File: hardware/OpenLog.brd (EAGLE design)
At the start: 17.8 x 19.1 mm, 20 parts, among them Q1 16MHZ, U1 ATMEGA328P_TQFP, U2 3.3V MIC5205, U3 microSD Socket

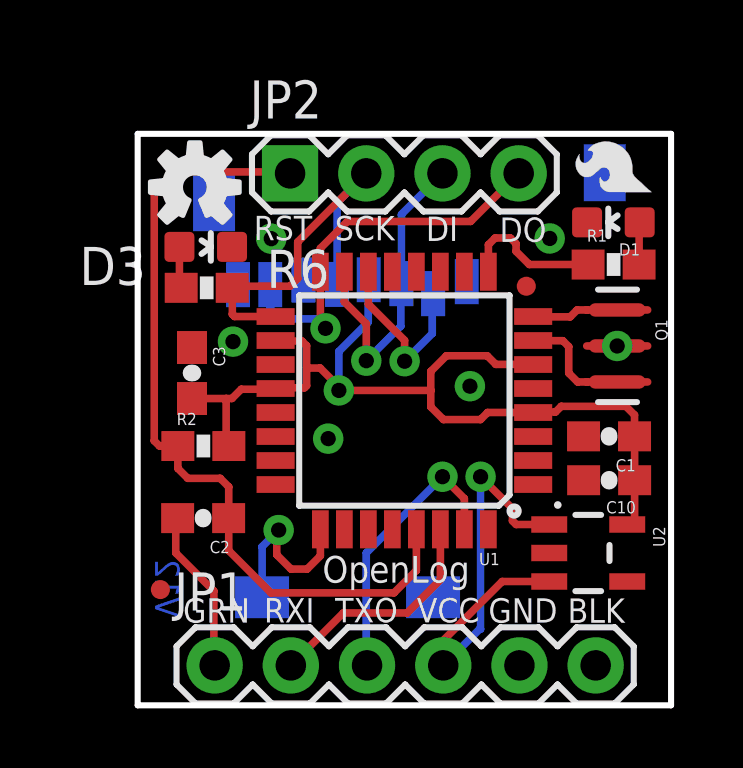
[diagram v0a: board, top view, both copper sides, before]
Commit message: Added Test point , removed OSHW logo
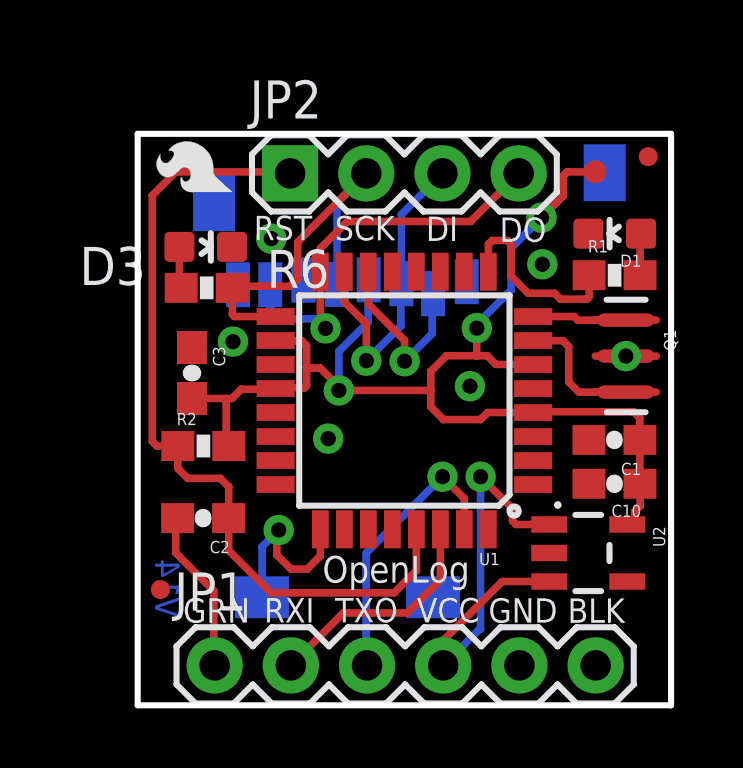
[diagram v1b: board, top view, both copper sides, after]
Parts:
- removed LOGO2: OSHW-LOGOS, SparkFun-Aesthetics:OSHW-LOGO-S
- added TP1: TEST-POINT3, SparkFun-Passives:PAD.03X.03
- moved LOGO1 14.0 mm to (22.6, 6.63)
- moved FID1 5.93 mm to (36.1, 8.13)
- moved Q1 0.44 mm to (35.3, 1.48)
- moved D1 0.38 mm to (35.0, 5.56)
- moved R1 0.36 mm to (34.9, 4.18)
- moved C1 0.21 mm to (34.9, -1.31)
- moved C10 0.21 mm to (34.9, -2.78)
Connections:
- net 3.3V: now also TP1.P$1
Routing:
- net 3.3V: track 32.8 -> 41.3 mm, vias 1 -> 3
- net N$4: track 4.83 -> 6.51 mm
- net N$1: track 1.89 -> 3.14 mm
- net N$2: track 2.87 -> 3.48 mm
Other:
- board text added: "V14"
- board text removed: "V12"

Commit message: Headers moved on grid.
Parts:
- moved JP1 0.07 mm to (21.6, -8.89)
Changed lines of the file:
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@@
 <setting verticaltext="up"/>
 </settings>
-<grid distance="0.05" unitdist="inch" unit="inch" style="lines" multiple="1" display="yes" altdistance="0.0001" altunitdist="inch" altunit="inch"/>
+<grid distance="0.05" unitdist="inch" unit="inch" style="lines" multiple="1" display="yes" altdistance="0.005" altunitdist="inch" altunit="inch"/>
 <layers>
 <layer number="1" name="Top" color="4" fill="1" visible="yes" active="yes"/>
@@
 <layer number="47" name="Measures" color="7" fill="1" visible="no" active="yes"/>
 <layer number="48" name="Document" color="7" fill="1" visible="no" active="yes"/>
-<layer number="49" name="Reference" color="7" fill="1" visible="yes" active="yes"/>
+<layer number="49" name="Reference" color="7" fill="1" visible="no" active="yes"/>
 <layer number="50" name="dxf" color="7" fill="1" visible="no" active="yes"/>
 <layer number="51" name="tDocu" color="6" fill="1" visible="yes" active="yes"/>
@@
 <attribute name="PROD_ID" value="XTAL-08900" x="35.321240625" y="1.48081875" size="1.778" layer="27" rot="R270" display="off"/>
 </element>
-<element name="JP1" library="SparkFun" package="1X06" value="Serial Connection" x="21.6154" y="-8.8290375"/>
+<element name="JP1" library="SparkFun" package="1X06" value="Serial Connection" x="21.59" y="-8.89"/>
 <element name="C2" library="SparkFun-Capacitors" package="0603-CAP" value="0.1uF" x="21.231859375" y="-3.919221875" rot="R180">
 <attribute name="PROD_ID" value="CAP-00810" x="21.231859375" y="-3.919221875" size="1.778" layer="27" rot="R180" display="off"/>
@@
 <attribute name="VALUE" value="1.0uF" x="34.9402375" y="-1.313175" size="1.778" layer="27" rot="R180" display="off"/>
 </element>
-<element name="JP2" library="SparkFun" package="1X04" value="" x="24.13" y="7.571740625"/>
+<element name="JP2" library="SparkFun" package="1X04" value="" x="24.13" y="7.62"/>
 <element name="U1" library="SparkFun-DigitalIC" package="TQFP32-08" value="ATMEGA328P_TQFP" x="27.94" y="0" rot="R180">
 <attribute name="PROD_ID" value="IC-09069" x="27.94" y="0" size="0.8128" layer="27" font="vector" ratio="15" rot="R180" display="off"/>
@@
 <contactref element="U1" pad="17"/>
 <wire x1="22.204678125" y1="3.753225" x2="22.201240625" y2="3.7566625" width="0.254" layer="1"/>
-<wire x1="25.69464375" y1="3.870953125" x2="25.69464375" y2="6.596384375" width="0.254" layer="16"/>
-<wire x1="25.69464375" y1="6.596384375" x2="26.67" y2="7.571740625" width="0.254" layer="16"/>
-<wire x1="24.384" y1="4.064" x2="24.384" y2="5.285740625" width="0.254" layer="1"/>
-<wire x1="24.384" y1="5.285740625" x2="26.67" y2="7.571740625" width="0.254" layer="1"/>
+<wire x1="25.69464375" y1="3.870953125" x2="25.69464375" y2="6.64464375" width="0.254" layer="16"/>
+<wire x1="24.384" y1="4.064" x2="24.384" y2="5.334" width="0.254" layer="1"/>
 <wire x1="23.6474" y1="2.8" x2="22.2799625" y2="2.8" width="0.254" layer="1"/>
 <wire x1="22.2799625" y1="2.8" x2="22.20468125" y2="2.87528125" width="0.254" layer="1"/>
@@
 <wire x1="24.13" y1="3.81" x2="22.254578125" y2="3.81" width="0.254" layer="1"/>
 <wire x1="22.254578125" y1="3.81" x2="22.201240625" y2="3.7566625" width="0.254" layer="1"/>
+<wire x1="24.384" y1="5.334" x2="26.67" y2="7.62" width="0.254" layer="1"/>
+<wire x1="25.69464375" y1="6.64464375" x2="26.67" y2="7.62" width="0.254" layer="16"/>
 </signal>
 <signal name="MISO">
@@
 <contactref element="U1" pad="16"/>
 <wire x1="25.14" y1="5.074" x2="25.14" y2="4.2926" width="0.254" layer="1"/>
-<wire x1="30.147259375" y1="5.969" x2="31.75" y2="7.571740625" width="0.254" layer="1"/>
 <wire x1="23.45181875" y1="3.086103125" x2="23.815040625" y2="2.72288125" width="0.254" layer="16"/>
 <wire x1="23.815040625" y1="2.72288125" x2="24.99360625" y2="2.72288125" width="0.254" layer="16"/>
@@
 <wire x1="23.45181875" y1="3.086103125" x2="23.45181875" y2="3.846415625" width="0.254" layer="16"/>
 <wire x1="23.45181875" y1="3.846415625" x2="23.4672125" y2="3.861809375" width="0.254" layer="16"/>
+<wire x1="30.147259375" y1="5.969" x2="30.147259375" y2="6.017259375" width="0.254" layer="1"/>
+<wire x1="30.147259375" y1="6.017259375" x2="31.75" y2="7.62" width="0.254" layer="1"/>
 </signal>
 <signal name="MOSI">
@@
 <wire x1="27.82149375" y1="2.479915625" x2="27.82149375" y2="3.876034375" width="0.254" layer="16"/>
 <wire x1="27.82149375" y1="3.876034375" x2="27.8418125" y2="3.896353125" width="0.254" layer="16"/>
-<wire x1="27.8418125" y1="3.896353125" x2="27.8418125" y2="6.203553125" width="0.254" layer="16"/>
-<wire x1="27.8418125" y1="6.203553125" x2="29.21" y2="7.571740625" width="0.254" layer="16"/>
+<wire x1="27.8418125" y1="3.896353125" x2="27.8418125" y2="6.2518125" width="0.254" layer="16"/>
+<wire x1="27.8418125" y1="6.2518125" x2="29.21" y2="7.62" width="0.254" layer="16"/>
 </signal>
 <signal name="N$7">
@@
 <contactref element="U1" pad="31"/>
 <wire x1="29.94" y1="-3.27" x2="29.94" y2="-4.2926" width="0.254" layer="1"/>
-<wire x1="26.67" y1="-5.08" x2="26.67" y2="-8.8036375" width="0.254" layer="16"/>
-<wire x1="26.67" y1="-8.8036375" x2="26.6954" y2="-8.8290375" width="0.254" layer="16"/>
+<wire x1="26.67" y1="-5.08" x2="26.67" y2="-8.89" width="0.254" layer="16"/>
 </signal>
 <signal name="RAW" class="1">
@@
 <wire x1="31.54171875" y1="-3.60171875" x2="30.48" y2="-2.54" width="0.254" layer="1"/>
 <wire x1="30.48" y1="-7.62" x2="30.4444375" y2="-7.62" width="0.254" layer="16"/>
-<wire x1="30.4444375" y1="-7.62" x2="29.2354" y2="-8.8290375" width="0.254" layer="16"/>
-<wire x1="29.2354" y1="-8.8290375" x2="29.2354" y2="-7.99591875" width="0.254" layer="1"/>
 <wire x1="29.2354" y1="-7.99591875" x2="31.19881875" y2="-6.0325" width="0.254" layer="1"/>
 <wire x1="31.19881875" y1="-6.0325" x2="32.76888125" y2="-6.0325" width="0.254" layer="1"/>
 <wire x1="32.76888125" y1="-6.0325" x2="32.768921875" y2="-6.032540625" width="0.254" layer="1"/>
+<wire x1="29.2354" y1="-7.99591875" x2="29.2354" y2="-8.8646" width="0.254" layer="1"/>
+<wire x1="29.2354" y1="-8.8646" x2="29.21" y2="-8.89" width="0.254" layer="1"/>
+<wire x1="30.4444375" y1="-7.62" x2="30.4444375" y2="-7.6555625" width="0.254" layer="16"/>
+<wire x1="30.4444375" y1="-7.6555625" x2="29.21" y2="-8.89" width="0.254" layer="16"/>
 </signal>
 <signal name="N$1">
@@
 <wire x1="20.32" y1="-5.08" x2="20.32" y2="-3.98108125" width="0.254" layer="1"/>
 <wire x1="20.32" y1="-3.98108125" x2="20.381859375" y2="-3.919221875" width="0.254" layer="1"/>
-<wire x1="21.59" y1="-6.35" x2="21.59" y2="-8.8036375" width="0.254" layer="1"/>
-<wire x1="21.59" y1="-8.8036375" x2="21.6154" y2="-8.8290375" width="0.254" layer="1"/>
+<wire x1="21.59" y1="-6.35" x2="21.59" y2="-8.89" width="0.254" layer="1"/>
 </signal>
 <signal name="RXI">
@@
 <wire x1="29.14" y1="-5.9780375" x2="28.03651875" y2="-7.08151875" width="0.254" layer="1"/>
 <wire x1="28.03651875" y1="-7.08151875" x2="25.90291875" y2="-7.08151875" width="0.254" layer="1"/>
-<wire x1="25.90291875" y1="-7.08151875" x2="24.1554" y2="-8.8290375" width="0.254" layer="1"/>
+<wire x1="25.90291875" y1="-7.08151875" x2="25.90291875" y2="-7.11708125" width="0.254" layer="1"/>
+<wire x1="25.90291875" y1="-7.11708125" x2="24.13" y2="-8.89" width="0.254" layer="1"/>
 </signal>
 <signal name="RST">
@@
 <wire x1="22.0853" y1="-5.001259375" x2="22.0853" y2="-3.9226625" width="0.254" layer="1"/>
 <wire x1="22.0853" y1="-3.9226625" x2="22.081859375" y2="-3.919221875" width="0.254" layer="1"/>
-<wire x1="20.32" y1="7.62" x2="24.081740625" y2="7.62" width="0.254" layer="1"/>
-<wire x1="24.081740625" y1="7.62" x2="24.13" y2="7.571740625" width="0.254" layer="1"/>
+<wire x1="20.32" y1="7.62" x2="24.13" y2="7.62" width="0.254" layer="1"/>
 <wire x1="20.38948125" y1="-1.51638125" x2="19.69008125" y2="-1.51638125" width="0.254" layer="1"/>
 <wire x1="19.69008125" y1="-1.51638125" x2="19.53768125" y2="-1.36398125" width="0.254" layer="1"/>

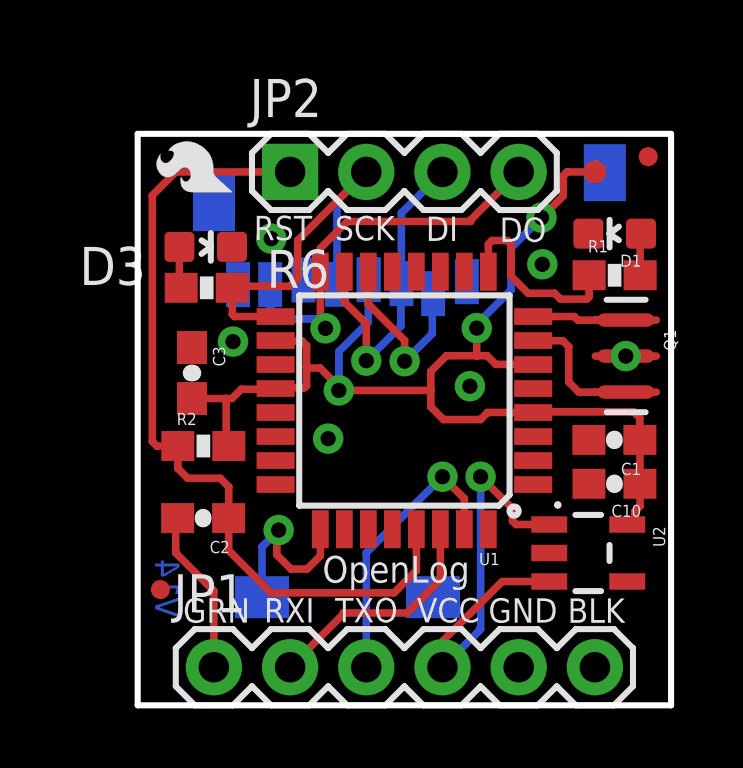
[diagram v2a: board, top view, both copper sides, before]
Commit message: Added OSHW logo, fixed trace
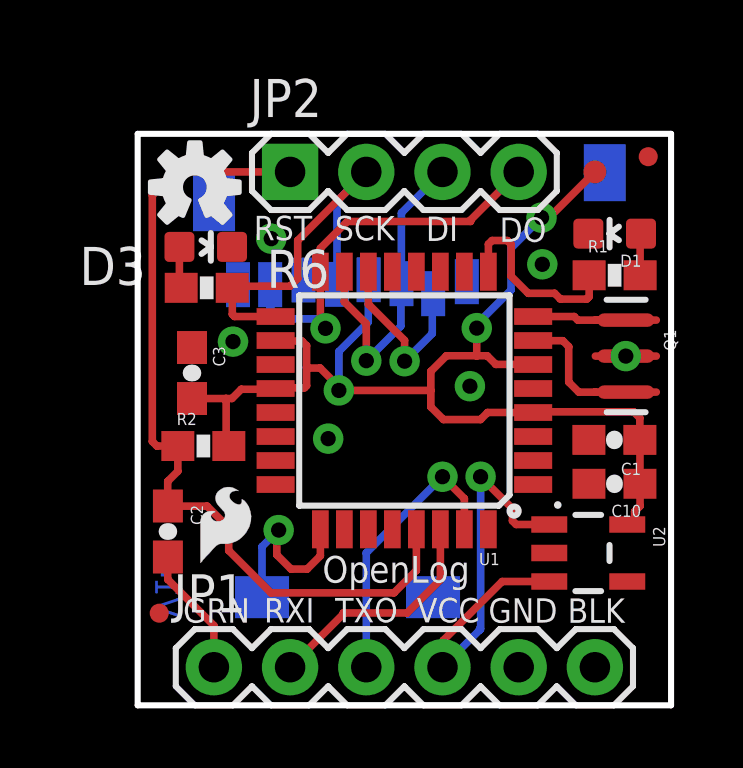
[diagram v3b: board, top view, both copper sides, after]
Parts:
- added LOGO2: OSHW-LOGOS, SparkFun-Aesthetics:OSHW-LOGO-S
- moved LOGO1 12.5 mm to (20.8, -5.78), turned to 0 degrees
- moved C2 1.26 mm to (20.1, -4.37), turned to 270 degrees
- moved FID2 0.79 mm to (19.8, -7.09)
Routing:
- net DTR: track 5.52 -> 4.31 mm
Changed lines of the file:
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@@
 <setting verticaltext="up"/>
 </settings>
-<grid distance="0.05" unitdist="inch" unit="inch" style="lines" multiple="1" display="yes" altdistance="0.005" altunitdist="inch" altunit="inch"/>
+<grid distance="0.05" unitdist="inch" unit="inch" style="lines" multiple="1" display="yes" altdistance="0.0001" altunitdist="inch" altunit="inch"/>
 <layers>
 <layer number="1" name="Top" color="4" fill="1" visible="yes" active="yes"/>
@@
 </element>
 <element name="JP1" library="SparkFun" package="1X06" value="Serial Connection" x="21.59" y="-8.89"/>
-<element name="C2" library="SparkFun-Capacitors" package="0603-CAP" value="0.1uF" x="21.231859375" y="-3.919221875" rot="R180">
-<attribute name="PROD_ID" value="CAP-00810" x="21.231859375" y="-3.919221875" size="1.778" layer="27" rot="R180" display="off"/>
-<attribute name="VALUE" value="0.1uF" x="21.231859375" y="-3.919221875" size="1.778" layer="27" rot="R180" display="off"/>
+<element name="C2" library="SparkFun-Capacitors" package="0603-CAP" value="0.1uF" x="20.058384375" y="-4.366259375" rot="R270">
+<attribute name="PROD_ID" value="CAP-00810" x="20.058384375" y="-4.366259375" size="1.778" layer="27" rot="R270" display="off"/>
+<attribute name="VALUE" value="0.1uF" x="20.058384375" y="-4.366259375" size="1.778" layer="27" rot="R270" display="off"/>
 </element>
 <element name="U3" library="SparkFun-Connectors" package="MICROSD_1:1" value="microSD Socket" x="35.1155" y="-6.9570625" rot="MR0">
@@
 <attribute name="DESIGNER" value="NAME" x="-0.742121875" y="-25.4" size="1.778" layer="27" display="off"/>
 </element>
-<element name="LOGO1" library="SparkFun-Aesthetics" package="SFE_LOGO_FLAME_.1" value="SFE_LOGO_FLAME.1_INCH" x="22.5704375" y="6.62685625" rot="R90"/>
+<element name="LOGO1" library="SparkFun-Aesthetics" package="SFE_LOGO_FLAME_.1" value="SFE_LOGO_FLAME.1_INCH" x="20.822915625" y="-5.775959375"/>
 <element name="FID1" library="SparkFun-Aesthetics" package="MICRO-FIDUCIAL" value="FIDUCIALUFIDUCIAL" x="36.068" y="8.128"/>
-<element name="FID2" library="SparkFun-Aesthetics" package="MICRO-FIDUCIAL" value="FIDUCIALUFIDUCIAL" x="19.80691875" y="-6.301740625"/>
+<element name="FID2" library="SparkFun-Aesthetics" package="MICRO-FIDUCIAL" value="FIDUCIALUFIDUCIAL" x="19.76881875" y="-7.0891375"/>
 <element name="TP1" library="SparkFun-Passives" package="PAD.03X.03" value="TEST-POINT3" x="34.29" y="7.62"/>
+<element name="LOGO2" library="SparkFun-Aesthetics" package="OSHW-LOGO-S" value="OSHW-LOGOS" x="20.955" y="7.112"/>
 </elements>
 <signals>
@@
 <contactref element="JP1" pad="1"/>
 <contactref element="C2" pad="2"/>
-<wire x1="21.59" y1="-6.35" x2="20.32" y2="-5.08" width="0.254" layer="1"/>
-<wire x1="20.32" y1="-5.08" x2="20.32" y2="-3.98108125" width="0.254" layer="1"/>
-<wire x1="20.32" y1="-3.98108125" x2="20.381859375" y2="-3.919221875" width="0.254" layer="1"/>
-<wire x1="21.59" y1="-6.35" x2="21.59" y2="-8.89" width="0.254" layer="1"/>
+<wire x1="21.59" y1="-8.89" x2="21.59" y2="-7.50061875" width="0.254" layer="1"/>
+<wire x1="21.59" y1="-7.50061875" x2="20.0533" y2="-5.96391875" width="0.254" layer="1"/>
+<wire x1="20.0533" y1="-5.96391875" x2="20.0533" y2="-5.22134375" width="0.254" layer="1"/>
+<wire x1="20.0533" y1="-5.22134375" x2="20.058384375" y2="-5.216259375" width="0.254" layer="1"/>
 </signal>
 <signal name="RXI">
@@
 <contactref element="JP2" pad="1"/>
 <contactref element="U1" pad="29"/>
-<wire x1="20.38948125" y1="-1.51638125" x2="20.38948125" y2="-2.264040625" width="0.254" layer="1"/>
-<wire x1="20.38948125" y1="-2.264040625" x2="20.71878125" y2="-2.593340625" width="0.254" layer="1"/>
-<wire x1="20.71878125" y1="-2.593340625" x2="21.800821875" y2="-2.593340625" width="0.254" layer="1"/>
-<wire x1="21.800821875" y1="-2.593340625" x2="22.0853" y2="-2.87781875" width="0.254" layer="1"/>
-<wire x1="22.0853" y1="-2.87781875" x2="22.0853" y2="-3.91578125" width="0.254" layer="1"/>
-<wire x1="22.0853" y1="-3.91578125" x2="22.081859375" y2="-3.919221875" width="0.254" layer="1"/>
 <wire x1="28.34" y1="-4.2926" x2="28.34" y2="-5.66551875" width="0.254" layer="1"/>
 <wire x1="28.34" y1="-5.66551875" x2="27.594559375" y2="-6.410959375" width="0.254" layer="1"/>
 <wire x1="27.594559375" y1="-6.410959375" x2="23.495" y2="-6.410959375" width="0.254" layer="1"/>
 <wire x1="23.495" y1="-6.410959375" x2="22.0853" y2="-5.001259375" width="0.254" layer="1"/>
-<wire x1="22.0853" y1="-5.001259375" x2="22.0853" y2="-3.9226625" width="0.254" layer="1"/>
-<wire x1="22.0853" y1="-3.9226625" x2="22.081859375" y2="-3.919221875" width="0.254" layer="1"/>
 <wire x1="20.32" y1="7.62" x2="24.13" y2="7.62" width="0.254" layer="1"/>
 <wire x1="20.38948125" y1="-1.51638125" x2="19.69008125" y2="-1.51638125" width="0.254" layer="1"/>
@@
 <wire x1="19.53768125" y1="-1.36398125" x2="19.53768125" y2="6.83768125" width="0.254" layer="1"/>
 <wire x1="19.53768125" y1="6.83768125" x2="20.32" y2="7.62" width="0.254" layer="1"/>
+<wire x1="22.0853" y1="-5.001259375" x2="22.0853" y2="-4.2418" width="0.254" layer="1"/>
+<wire x1="22.0853" y1="-4.2418" x2="21.363940625" y2="-3.520440625" width="0.254" layer="1"/>
+<wire x1="21.363940625" y1="-3.520440625" x2="20.062565625" y2="-3.520440625" width="0.254" layer="1"/>
+<wire x1="20.062565625" y1="-3.520440625" x2="20.058384375" y2="-3.516259375" width="0.254" layer="1"/>
+<wire x1="20.0524" y1="-2.6933" x2="20.38858125" y2="-2.35711875" width="0.254" layer="1"/>
+<wire x1="20.38858125" y1="-2.35711875" x2="20.38858125" y2="-1.51728125" width="0.254" layer="1"/>
+<wire x1="20.38858125" y1="-1.51728125" x2="20.38948125" y2="-1.51638125" width="0.254" layer="1"/>
+<wire x1="20.0524" y1="-2.6933" x2="20.0524" y2="-3.510275" width="0.254" layer="1"/>
+<wire x1="20.0524" y1="-3.510275" x2="20.058384375" y2="-3.516259375" width="0.254" layer="1"/>
 </signal>
 <signal name="N$3">
@@
 <wire x1="31.496" y1="3.683" x2="31.496" y2="5.08" width="0.254" layer="16"/>
 <wire x1="31.496" y1="5.08" x2="32.512" y2="6.096" width="0.254" layer="16"/>
-<wire x1="32.512" y1="6.096" x2="33.238440625" y2="6.822440625" width="0.254" layer="1"/>
-<wire x1="33.238440625" y1="6.822440625" x2="33.238440625" y2="7.495540625" width="0.254" layer="1"/>
-<wire x1="33.238440625" y1="7.495540625" x2="33.3629" y2="7.62" width="0.254" layer="1"/>
-<wire x1="33.3629" y1="7.62" x2="34.29" y2="7.62" width="0.254" layer="1"/>
 <wire x1="35.61498125" y1="-4.132540625" x2="35.61498125" y2="-3.6991375" width="0.254" layer="1"/>
 <wire x1="35.61498125" y1="-3.6991375" x2="35.79621875" y2="-3.5179" width="0.254" layer="1"/>
@@
 <wire x1="35.7886" y1="-0.581659375" x2="35.7886" y2="-1.3115375" width="0.254" layer="1"/>
 <wire x1="35.7886" y1="-1.3115375" x2="35.7902375" y2="-1.313175" width="0.254" layer="1"/>
+<wire x1="32.512" y1="6.096" x2="32.766" y2="6.096" width="0.254" layer="1"/>
+<wire x1="32.766" y1="6.096" x2="34.29" y2="7.62" width="0.254" layer="1"/>
 </signal>
 </signals>
